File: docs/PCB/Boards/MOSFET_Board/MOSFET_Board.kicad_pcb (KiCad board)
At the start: 2 copper layers, 57.8 x 26.3 mm, 20 parts, among them IC1 TC4420CPA, J1 COM, J2 PWR, J3 BULB, Q1 IRLZ44N, U1 L78L12_TO92

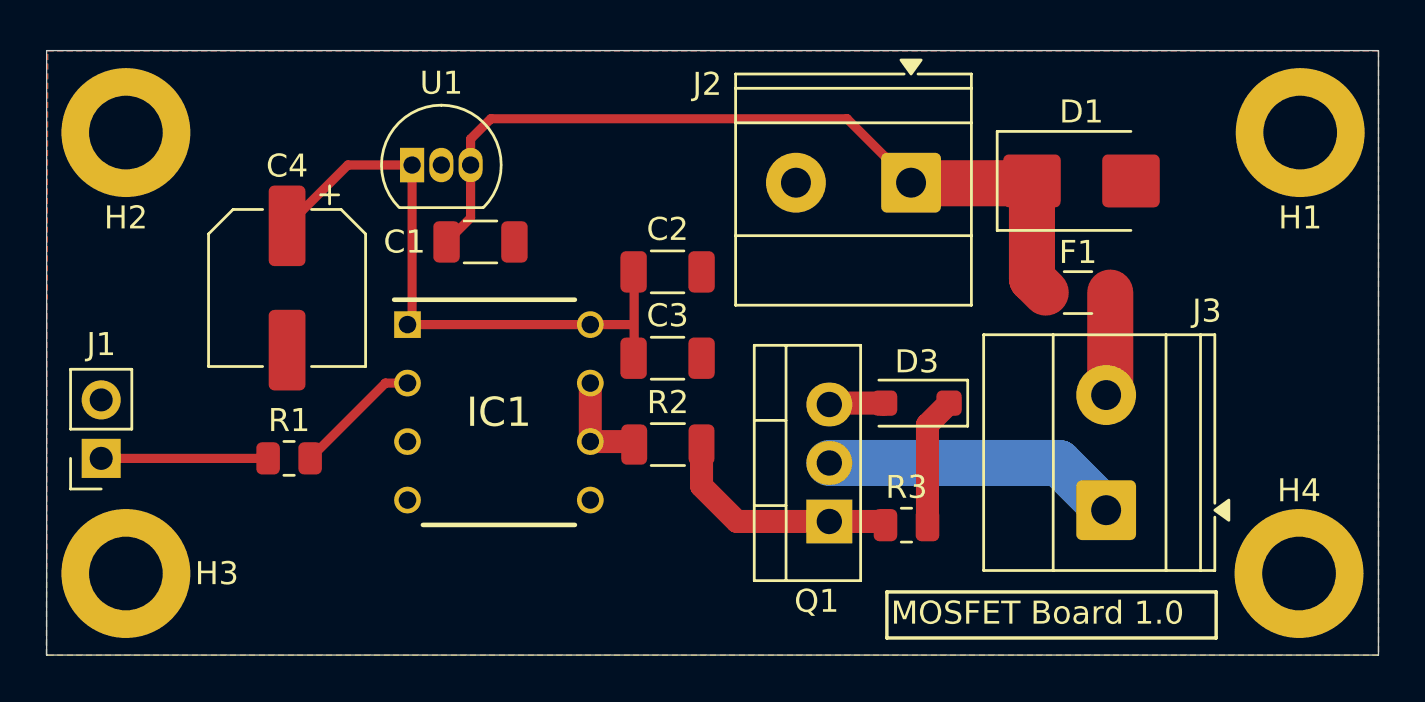
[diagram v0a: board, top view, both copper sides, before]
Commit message: Test program added, can protocol added.
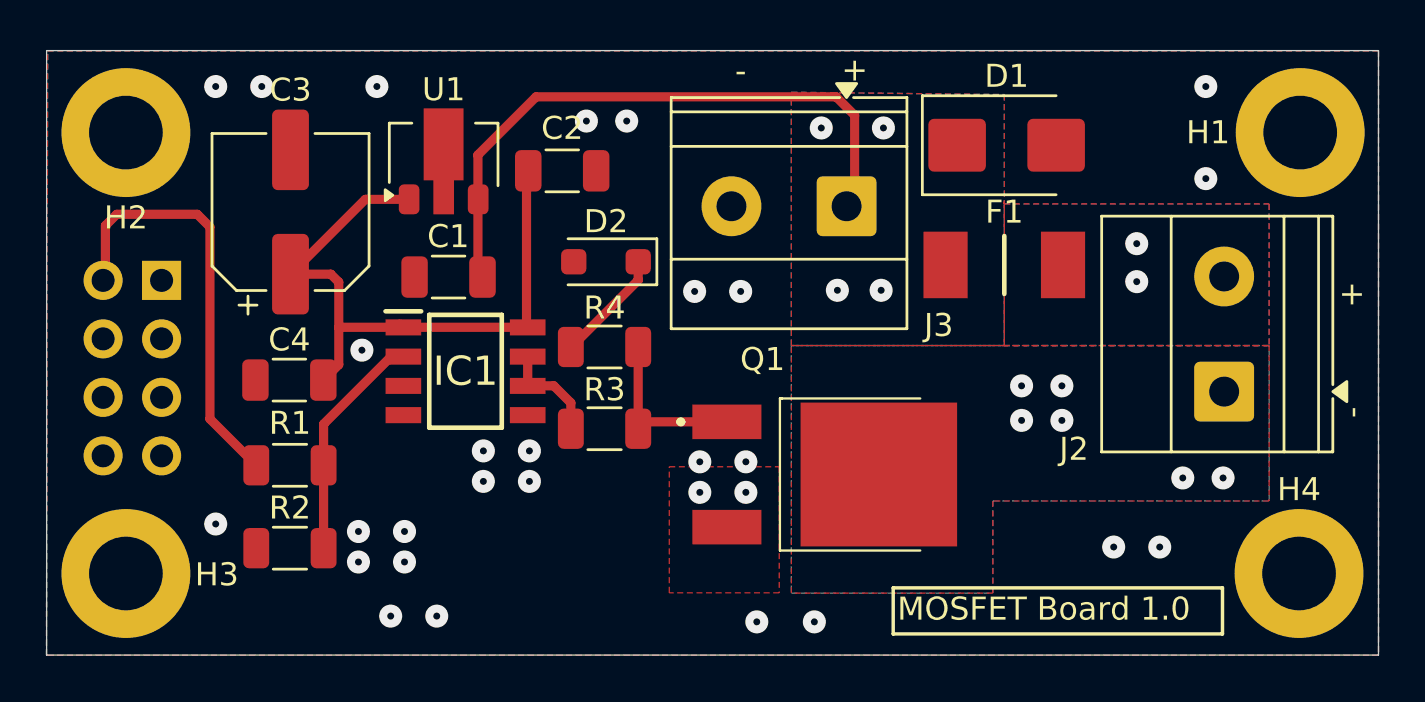
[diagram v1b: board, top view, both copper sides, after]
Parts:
- removed D3: BZX55C12, Diode_SMD:D_SOD-123F
- added D2: BZX55C12, Diode_SMD:D_SOD-123F, F.Cu at (145.9, 77.6)
- added R4: 100K, Resistor_SMD:R_1206_3216Metric, F.Cu at (145.9, 81.3)
- C3: value 100nF -> 10uF; footprint Capacitor_SMD:C_1206_3216Metric -> Capacitor_SMD:CP_Elec_6.3x5.8
- C4: value 10uF -> 100nF; footprint Capacitor_SMD:CP_Elec_6.3x5.8 -> Capacitor_SMD:C_1206_3216Metric
- F1: value 5A -> TR1-2410TD5-R; footprint Fuse:Fuse_1206_3216Metric -> Library:FUSC6127X287N
- IC1: value TC4420CPA -> TC4420EOA; footprint Library:DIP794W56P254L946H432Q8N -> Library:SOIC127P600X175-8N
- J1: footprint Connector_PinSocket_2.54mm:PinSocket_1x02_P2.54mm_Vertical -> Connector_PinHeader_2.54mm:PinHeader_2x04_P2.54mm_Vertical; moved to B.Cu
- J2: value PWR -> BULB
- J3: value BULB -> PWR
- Q1: value IRLZ44N -> AOD4184A; footprint Package_TO_SOT_THT:TO-220-3_Vertical -> Library:AOD4185
- R1: value 100R 125mW -> 100R; footprint Resistor_SMD:R_0805_2012Metric -> Resistor_SMD:R_1206_3216Metric
- R2: value 10R 250mW -> 47K
- R3: value 100K 250mW -> 10R; footprint Resistor_SMD:R_0805_2012Metric -> Resistor_SMD:R_1206_3216Metric
- U1: value L78L12_TO92 -> L78L12_SOT89; footprint Package_TO_SOT_THT:TO-92_Inline -> Package_TO_SOT_SMD:SOT-89-3
- moved C3 17.6 mm to (132.2, 75.5), turned to 90 degrees
- moved J3 17.4 mm to (156.4, 75.2), turned to 180 degrees
- moved R2 17.0 mm to (132.2, 90.0), turned to 180 degrees
- moved J2 16.3 mm to (172.8, 83.2), turned to 90 degrees
- moved R3 13.8 mm to (145.9, 84.9)
- moved J1 8.16 mm to (126.7, 78.4)
- moved C2 6.34 mm to (144.1, 73.7)
- moved C4 4.00 mm to (132.2, 82.8), turned to 180 degrees
- moved D1 3.60 mm to (163.3, 72.5)
- moved F1 3.42 mm to (163.2, 77.8)
- moved IC1 2.30 mm to (139.8, 82.4)
- moved C1 2.06 mm to (139.1, 78.3), turned to 180 degrees
- moved Q1 2.06 mm to (155.4, 86.8), turned to -90 degrees
- moved U1 1.45 mm to (138.9, 73.0), turned to 90 degrees
- moved R1 0.30 mm to (132.2, 86.5)
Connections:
- F1 pad 1: Net-(J3-Pin_2) -> Net-(J2-Pin_2)
- J1 pad 1: Net-(J1-Pin_1) -> unconnected-(J1-Pin_1-Pad1)
- J1 pad 2: GND -> Net-(J1-Pin_2)
- J2 pad 1: +12V -> Net-(J2-Pin_1)
- J2 pad 2: GND -> Net-(J2-Pin_2)
- J3 pad 1: Net-(J3-Pin_1) -> +12V
- J3 pad 2: Net-(J3-Pin_2) -> GND
- Q1 pad 2: Net-(J3-Pin_1) -> Net-(J2-Pin_1)
- Q1 pad 3: Net-(D3-A) -> GND
- R1 pad 1: Net-(J1-Pin_1) -> Net-(J1-Pin_2)
- R2 pad 1: Net-(IC1-OUTPUT_1) -> Net-(IC1-INPUT)
- R2 pad 2: Net-(Q1-G) -> GND
- R3 pad 1: Net-(Q1-G) -> Net-(IC1-OUTPUT_1)
- R3 pad 2: Net-(D3-K) -> Net-(Q1-G)
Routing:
- net Net-(J1-Pin_2): track 0.00 -> 18.6 mm
- net Net-(J3-Pin_1): track 13.0 -> 0.00 mm
- net +12V: track 35.7 -> 27.2 mm, vias 0 -> 4
- net Net-(J1-Pin_1): track 7.25 -> 0.00 mm
- net Net-(D3-K): track 5.69 -> 0.00 mm
- net Net-(D2-K): track 0.00 -> 4.93 mm
- net Net-(J3-Pin_2): track 4.62 -> 0.00 mm
- net Net-(IC1-INPUT): track 5.58 -> 10.1 mm
- net Net-(Q1-G): track 10.5 -> 7.12 mm
- net Net-(D3-A): track 2.39 -> 0.00 mm
- net +12V_STAB: track 27.0 -> 28.5 mm
- net Net-(J2-Pin_2): vias 0 -> 2
- net Net-(J2-Pin_1): vias 0 -> 6
- net GND: vias 0 -> 29
- added copper zone on B.Cu, net +12V
- added copper zone on F.Cu, net +12V
- added copper zone on B.Cu, net Net-(J2-Pin_1)
- added copper zone on F.Cu, net Net-(J2-Pin_1)
- added copper zone on B.Cu, net Net-(J2-Pin_2)
- added copper zone on F.Cu, net Net-(J2-Pin_2)
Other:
- board text added: "+"
- board text added: "-"

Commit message: Boards modified - tree and power boards added.
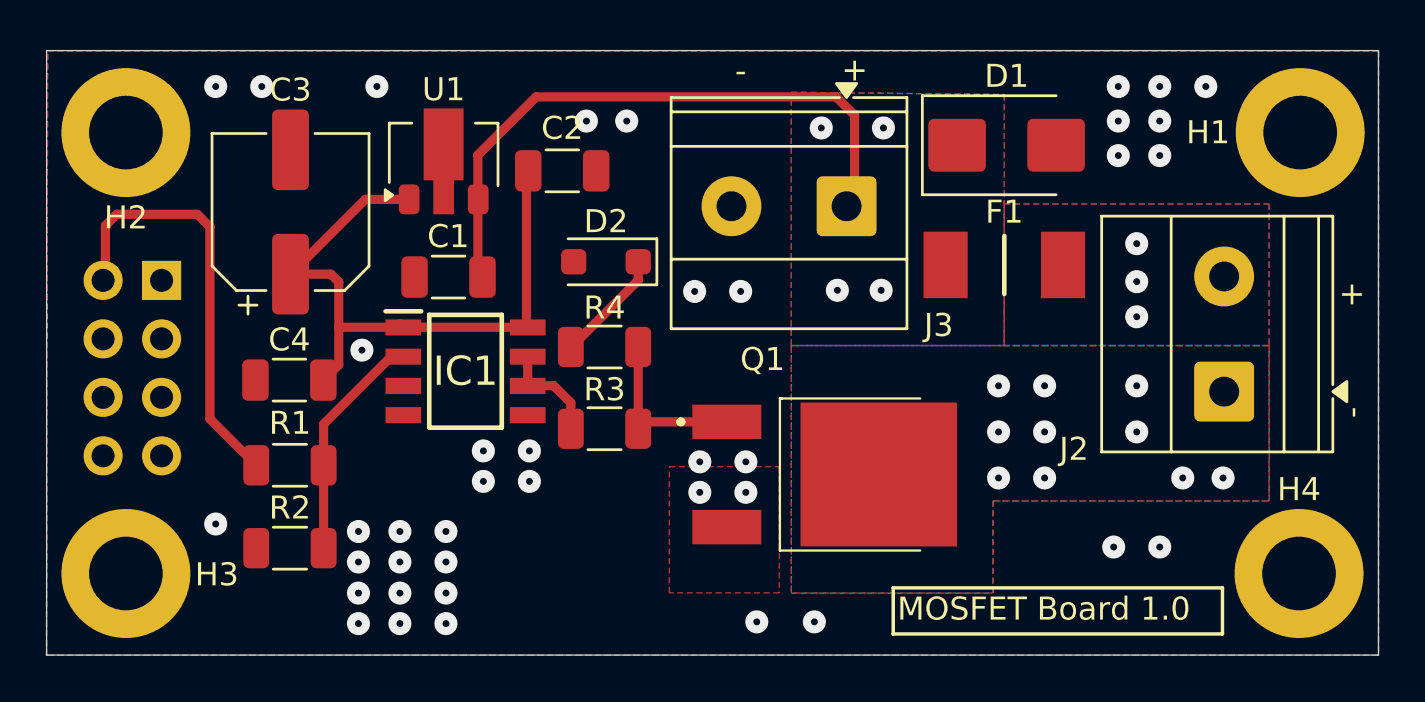
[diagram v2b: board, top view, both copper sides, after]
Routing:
- net Net-(J2-Pin_2): vias 2 -> 3
- net Net-(J2-Pin_1): vias 6 -> 10
- net GND: vias 29 -> 40
